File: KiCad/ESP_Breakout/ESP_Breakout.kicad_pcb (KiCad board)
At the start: 2 copper layers, 127 x 67 mm, 21 parts, among them J1 Conn_01x15_Socket, J2 Conn_01x15_Socket, J3 Conn_01x03_Pin, J4 Conn_01x03_Pin, J5 Conn_01x03_Pin, J6 Conn_01x03_Pin, J7 Conn_01x15_Socket, J8 Conn_01x15_Socket

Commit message: wiring progress
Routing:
- net +3.3V: track 10.0 -> 209.2 mm
- net /Drive_Ena+: track 10.0 -> 207.8 mm, vias 0 -> 4
- net GND: track 262.3 -> 459.1 mm, vias 0 -> 2
- net /Lift_Ena+: track 10.0 -> 205.6 mm, vias 0 -> 4
- net /Turn_Ena+: track 10.0 -> 195.0 mm, vias 0 -> 1
- net /Lift_Dir+: track 10.0 -> 189.1 mm, vias 0 -> 6
- net /Drive_Dir+: track 10.0 -> 166.2 mm, vias 0 -> 2
- net /Lift_Pul+: track 10.0 -> 159.7 mm, vias 0 -> 1
- net /Drive_Pul+: track 10.0 -> 132.2 mm, vias 0 -> 3
- net /Turn4_Pul+: track 10.0 -> 102.8 mm
- net /Turn4_Dir+: track 10.0 -> 83.3 mm
- net /Turn2_Dir+: track 10.0 -> 36.3 mm, vias 0 -> 1
- net /Turn3_Pul+: track 10.0 -> 35.9 mm, vias 0 -> 1
- net /Turn2_Pul+: track 10.0 -> 35.9 mm, vias 0 -> 1
- net /Turn1_Dir+: track 10.0 -> 33.2 mm, vias 0 -> 4
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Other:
- board size 127 x 67 mm -> 127 x 70.2 mm

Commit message: update
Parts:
- moved U1 91.2 mm to (69.0, 63.7)
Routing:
- net /Drive_Dir+: track 166.2 -> 251.2 mm
- net /Turn3_Dir+: track 10.0 -> 80.5 mm, vias 0 -> 2
- net /Drive_Pul+: track 132.2 -> 175.6 mm, vias 3 -> 4
- net GND: track 459.1 -> 483.4 mm
- net /Drive_Ena+: track 207.8 -> 206.0 mm
- net /Turn1_Dir+: track 33.2 -> 33.1 mm, vias 4 -> 3
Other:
- board text added: "NEON - MOTOR CONTROL BOARD CARROT"

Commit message: start of pheonix
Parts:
- added H1: MountingHole, MountingHole:MountingHole_2.5mm, F.Cu at (95.9, 48.8)
- added H2: MountingHole, MountingHole:MountingHole_2.5mm, F.Cu at (95.9, 113.5)
- added H3: MountingHole, MountingHole:MountingHole_2.5mm, F.Cu at (217.4, 48.8)
- added H4: MountingHole, MountingHole:MountingHole_2.5mm, F.Cu at (217.4, 113.5)
- moved U1 46.0 mm to (36.1, 95.8)

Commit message: commit
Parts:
- removed U1: ~, seniorDesign:MODULE_ESP32_DEVKIT_V1
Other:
- board text added: "3.3V"
- board text added: "GND"
- board text added: "NEON CARROT MOTOR CONTROL BOARD"
- board text removed: "NEON - MOTOR CONTROL BOARD CARROT"

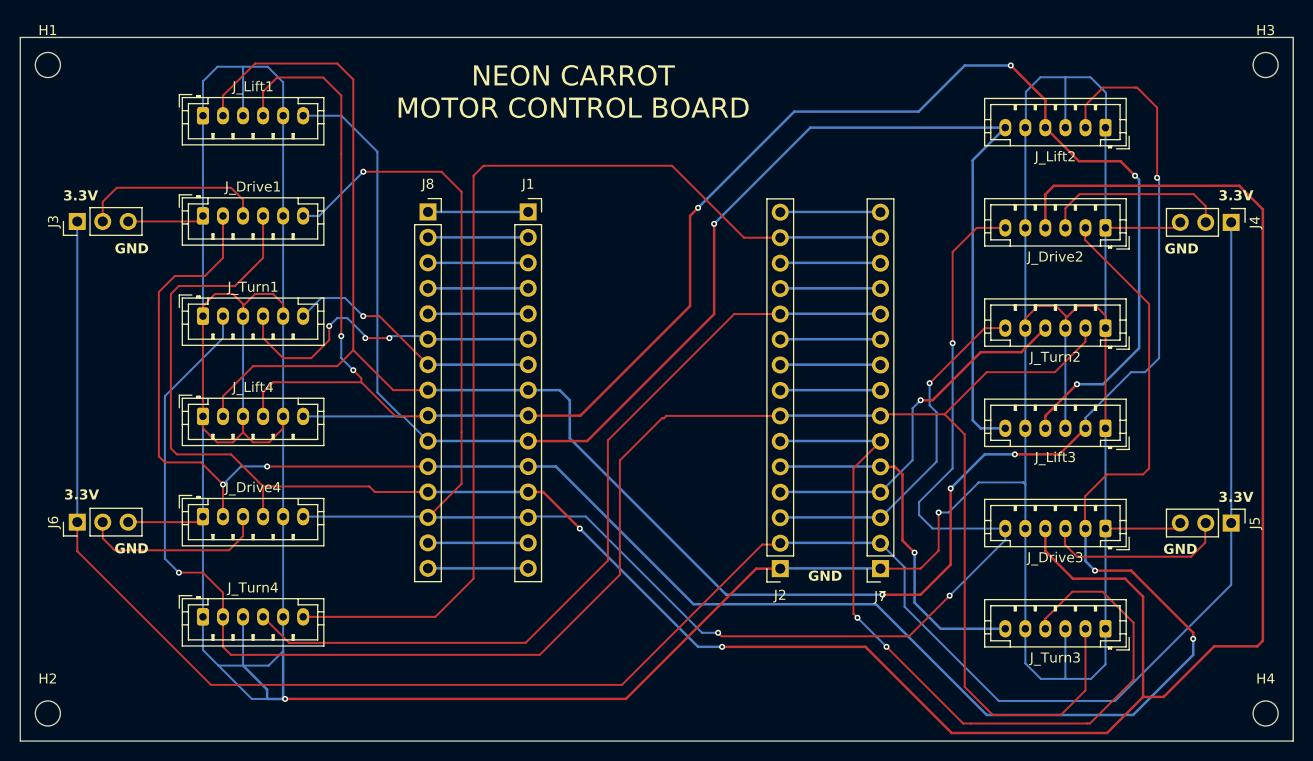
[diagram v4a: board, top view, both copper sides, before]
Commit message: changed mounting holes
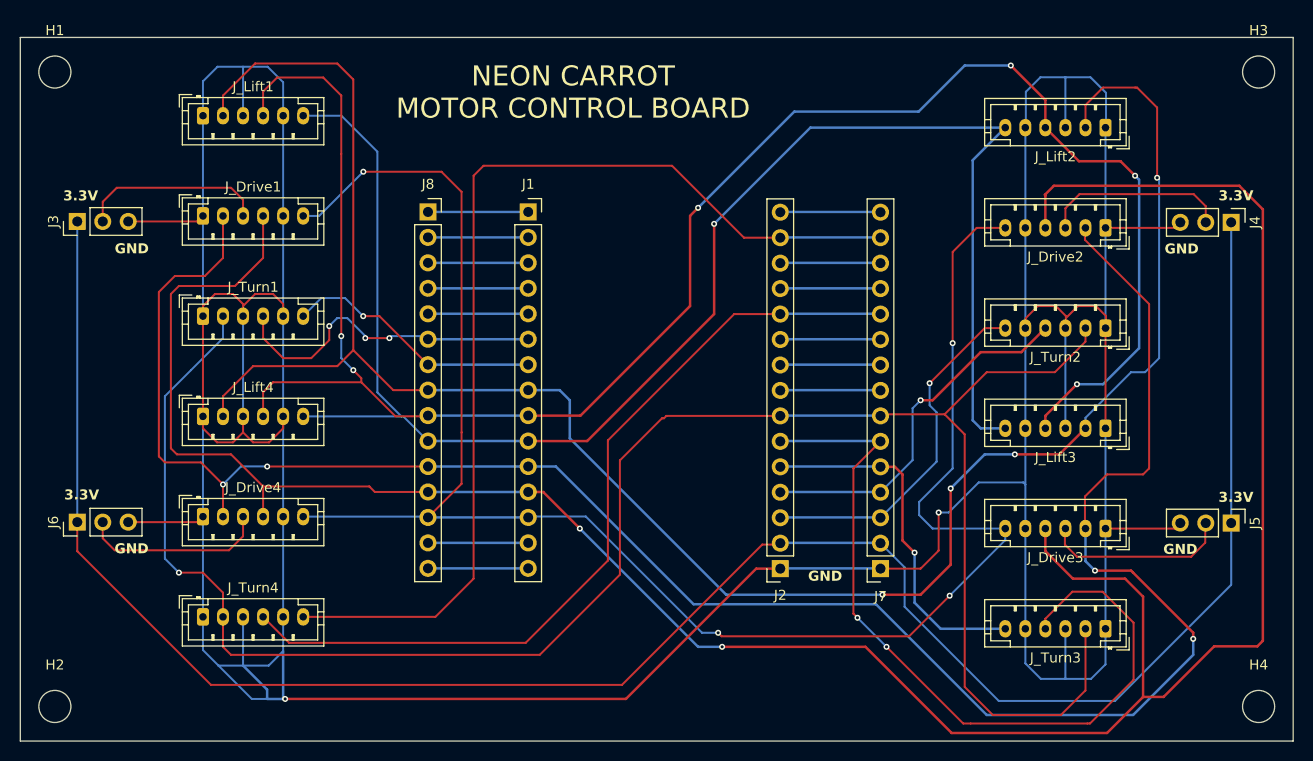
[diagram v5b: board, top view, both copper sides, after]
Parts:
- H1, H2, H3, H4: footprint MountingHole:MountingHole_2.5mm -> MountingHole:MountingHole_3.2mm_M3
- moved H3 0.99 mm to (216.7, 49.5)
- moved H4 0.99 mm to (216.7, 112.8)
- moved H1 0.99 mm to (96.6, 49.5)
- moved H2 0.99 mm to (96.6, 112.8)
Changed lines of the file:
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@@
 			)
 		)
-		(property "Datasheet" "~"
+		(property "Datasheet" "https://www.digikey.com/en/products/detail/w%C3%BCrth-elektronik/61300311121/4846825"
 			(at 0 0 90)
 			(layer "F.Fab")
@@
 		)
 	)
-	(footprint "MountingHole:MountingHole_2.5mm"
+	(footprint "MountingHole:MountingHole_3.2mm_M3"
 		(layer "F.Cu")
-		(at 217.425 48.75)
-		(descr "Mounting Hole 2.5mm, no annular, generated by kicad-footprint-generator mountinghole.py")
-		(tags "mountinghole")
+		(at 216.725 49.45)
+		(descr "Mounting Hole 3.2mm, M3, no annular, generated by kicad-footprint-generator mountinghole.py")
+		(tags "mountinghole M3")
 		(property "Reference" "H3"
-			(at 0 -3.45 0)
+			(at 0 -4.15 0)
 			(layer "F.SilkS")
 			(effects
@@
 		)
 		(property "Value" "MountingHole"
-			(at 0 3.45 0)
+			(at 0 4.15 0)
 			(layer "F.Fab")
 			(effects
@@
 		(fp_circle
 			(center 0 0)
-			(end 2.5 0)
+			(end 3.2 0)
 			(stroke
 				(width 0.15)
@@
 		(fp_circle
 			(center 0 0)
-			(end 2.75 0)
+			(end 3.45 0)
 			(stroke
 				(width 0.05)
@@
 		(pad "" np_thru_hole circle
 			(at 0 0)
-			(size 2.5 2.5)
-			(drill 2.5)
+			(size 3.2 3.2)
+			(drill 3.2)
 			(layers "*.Cu" "*.Mask")
 		)
@@
 			)
 		)
-		(property "Datasheet" ""
+		(property "Datasheet" "https://www.digikey.com/en/products/detail/jst-sales-america-inc/B6B-PH-K-S/926615"
 			(at 0 0 0)
 			(layer "F.Fab")
@@
 			)
 		)
-		(property "Datasheet" ""
+		(property "Datasheet" "https://www.digikey.com/en/products/detail/jst-sales-america-inc/B6B-PH-K-S/926615"
 			(at 0 0 0)
 			(layer "F.Fab")
@@
 			)
 		)
-		(property "Datasheet" "~"
+		(property "Datasheet" "https://www.digikey.com/en/products/detail/sullins-connector-solutions/PPTC151LFBN-RC/810153"
 			(at 0 0 0)
 			(layer "F.Fab")
@@
 		)
 	)
-	(footprint "MountingHole:MountingHole_2.5mm"
+	(footprint "MountingHole:MountingHole_3.2mm_M3"
 		(layer "F.Cu")
-		(at 95.925 48.75)
-		(descr "Mounting Hole 2.5mm, no annular, generated by kicad-footprint-generator mountinghole.py")
-		(tags "mountinghole")
+		(at 96.625 49.45)
+		(descr "Mounting Hole 3.2mm, M3, no annular, generated by kicad-footprint-generator mountinghole.py")
+		(tags "mountinghole M3")
 		(property "Reference" "H1"
-			(at 0 -3.45 0)
+			(at 0 -4.15 0)
 			(layer "F.SilkS")
 			(effects
@@
 		)
 		(property "Value" "MountingHole"
-			(at 0 3.45 0)
+			(at 0 4.15 0)
 			(layer "F.Fab")
 			(effects
@@
 		(fp_circle
 			(center 0 0)
-			(end 2.5 0)
+			(end 3.2 0)
 			(stroke
 				(width 0.15)
@@
 		(fp_circle
 			(center 0 0)
-			(end 2.75 0)
+			(end 3.45 0)
 			(stroke
 				(width 0.05)
@@
 		(pad "" np_thru_hole circle
 			(at 0 0)
-			(size 2.5 2.5)
-			(drill 2.5)
+			(size 3.2 3.2)
+			(drill 3.2)
 			(layers "*.Cu" "*.Mask")
 		)
@@
 			)
 		)
-		(property "Datasheet" ""
+		(property "Datasheet" "https://www.digikey.com/en/products/detail/jst-sales-america-inc/B6B-PH-K-S/926615"
 			(at 0 0 0)
 			(layer "F.Fab")
@@
 			)
 		)
-		(property "Datasheet" ""
+		(property "Datasheet" "https://www.digikey.com/en/products/detail/jst-sales-america-inc/B6B-PH-K-S/926615"
 			(at 0 0 0)
 			(layer "F.Fab")
@@
 			)
 		)
-		(property "Datasheet" ""
+		(property "Datasheet" "https://www.digikey.com/en/products/detail/jst-sales-america-inc/B6B-PH-K-S/926615"
 			(at 0 0 0)
 			(layer "F.Fab")
@@
 			)
 		)
-		(property "Datasheet" ""
+		(property "Datasheet" "https://www.digikey.com/en/products/detail/jst-sales-america-inc/B6B-PH-K-S/926615"
 			(at 0 0 0)
 			(layer "F.Fab")
@@
 			)
 		)
-		(property "Datasheet" "~"
+		(property "Datasheet" "https://www.digikey.com/en/products/detail/sullins-connector-solutions/PPTC151LFBN-RC/810153"
 			(at 0 0 0)
 			(layer "F.Fab")
@@
 			)
 		)
-		(property "Datasheet" ""
+		(property "Datasheet" "https://www.digikey.com/en/products/detail/jst-sales-america-inc/B6B-PH-K-S/926615"
 			(at 0 0 0)
 			(layer "F.Fab")
@@
 			)
 		)
-		(property "Datasheet" "~"
+		(property "Datasheet" "https://www.digikey.com/en/products/detail/w%C3%BCrth-elektronik/61300311121/4846825"
 			(at 0 0 90)
 			(layer "F.Fab")
@@
 			)
 		)
-		(property "Datasheet" "~"
+		(property "Datasheet" "https://www.digikey.com/en/products/detail/sullins-connector-solutions/PPTC151LFBN-RC/810153"
 			(at 0 0 0)
 			(layer "F.Fab")
@@
 		)
 	)
-	(footprint "MountingHole:MountingHole_2.5mm"
+	(footprint "MountingHole:MountingHole_3.2mm_M3"
 		(layer "F.Cu")
-		(at 95.925 113.45)
-		(descr "Mounting Hole 2.5mm, no annular, generated by kicad-footprint-generator mountinghole.py")
-		(tags "mountinghole")
+		(at 96.625 112.75)
+		(descr "Mounting Hole 3.2mm, M3, no annular, generated by kicad-footprint-generator mountinghole.py")
+		(tags "mountinghole M3")
 		(property "Reference" "H2"
-			(at 0 -3.45 0)
+			(at 0 -4.15 0)
 			(layer "F.SilkS")
 			(effects
@@
 		)
 		(property "Value" "MountingHole"
-			(at 0 3.45 0)
+			(at 0 4.15 0)
 			(layer "F.Fab")
 			(effects
@@
 		(fp_circle
 			(center 0 0)
-			(end 2.5 0)
+			(end 3.2 0)
 			(stroke
 				(width 0.15)
@@
 		(fp_circle
 			(center 0 0)
-			(end 2.75 0)
+			(end 3.45 0)
 			(stroke
 				(width 0.05)
@@
 		(pad "" np_thru_hole circle
 			(at 0 0)
-			(size 2.5 2.5)
-			(drill 2.5)
+			(size 3.2 3.2)
+			(drill 3.2)
 			(layers "*.Cu" "*.Mask")
 		)
 		(embedded_fonts no)
 	)
-	(footprint "MountingHole:MountingHole_2.5mm"
+	(footprint "MountingHole:MountingHole_3.2mm_M3"
 		(layer "F.Cu")
-		(at 217.425 113.45)
-		(descr "Mounting Hole 2.5mm, no annular, generated by kicad-footprint-generator mountinghole.py")
-		(tags "mountinghole")
+		(at 216.725 112.75)
+		(descr "Mounting Hole 3.2mm, M3, no annular, generated by kicad-footprint-generator mountinghole.py")
+		(tags "mountinghole M3")
 		(property "Reference" "H4"
-			(at 0 -3.45 0)
+			(at 0 -4.15 0)
 			(layer "F.SilkS")
 			(effects
@@
 		)
 		(property "Value" "MountingHole"
-			(at 0 3.45 0)
+			(at 0 4.15 0)
 			(layer "F.Fab")
 			(effects
@@
 		(fp_circle
 			(center 0 0)
-			(end 2.5 0)
+			(end 3.2 0)
 			(stroke
 				(width 0.15)
@@
 		(fp_circle
 			(center 0 0)
-			(end 2.75 0)
+			(end 3.45 0)
 			(stroke
 				(width 0.05)
@@
 		(pad "" np_thru_hole circle
 			(at 0 0)
-			(size 2.5 2.5)
-			(drill 2.5)
+			(size 3.2 3.2)
+			(drill 3.2)
 			(layers "*.Cu" "*.Mask")
 		)
@@
 			)
 		)
-		(property "Datasheet" "~"
+		(property "Datasheet" "https://www.digikey.com/en/products/detail/w%C3%BCrth-elektronik/61300311121/4846825"
 			(at 0 0 90)
 			(layer "F.Fab")
@@
 			)
 		)
-		(property "Datasheet" ""
+		(property "Datasheet" "https://www.digikey.com/en/products/detail/jst-sales-america-inc/B6B-PH-K-S/926615"
 			(at 0 0 0)
 			(layer "F.Fab")
@@
 			)
 		)
-		(property "Datasheet" ""
+		(property "Datasheet" "https://www.digikey.com/en/products/detail/jst-sales-america-inc/B6B-PH-K-S/926615"
 			(at 0 0 0)
 			(layer "F.Fab")
@@
 			)
 		)
-		(property "Datasheet" ""
+		(property "Datasheet" "https://www.digikey.com/en/products/detail/jst-sales-america-inc/B6B-PH-K-S/926615"
 			(at 0 0 0)
 			(layer "F.Fab")
@@
 			)
 		)
-		(property "Datasheet" ""
+		(property "Datasheet" "https://www.digikey.com/en/products/detail/jst-sales-america-inc/B6B-PH-K-S/926615"
 			(at 0 0 0)
 			(layer "F.Fab")
@@
 			)
 		)
-		(property "Datasheet" ""
+		(property "Datasheet" "https://www.digikey.com/en/products/detail/sullins-connector-solutions/PPTC151LFBN-RC/810153"
 			(at 0 0 0)
 			(layer "F.Fab")
@@
 			)
 		)
-		(property "Datasheet" "~"
+		(property "Datasheet" "https://www.digikey.com/en/products/detail/w%C3%BCrth-elektronik/61300311121/4846825"
 			(at 0 0 90)
 			(layer "F.Fab")
@@
 			)
 		)
-		(property "Datasheet" ""
+		(property "Datasheet" "https://www.digikey.com/en/products/detail/jst-sales-america-inc/B6B-PH-K-S/926615"
 			(at 0 0 0)
 			(layer "F.Fab")
